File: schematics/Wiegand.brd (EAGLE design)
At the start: 79 x 51.9 mm, 88 parts, among them J1 AVR_SPI_PRG_6PTH, U1 MOC3063, U2 MOC3063, U3 V_REG_LDOSMD, U4 ATMEGA168, U5 MOC3063, U6 MOC3063, U7 MOC3063, U8 MOC3063, Y1 16Mhz

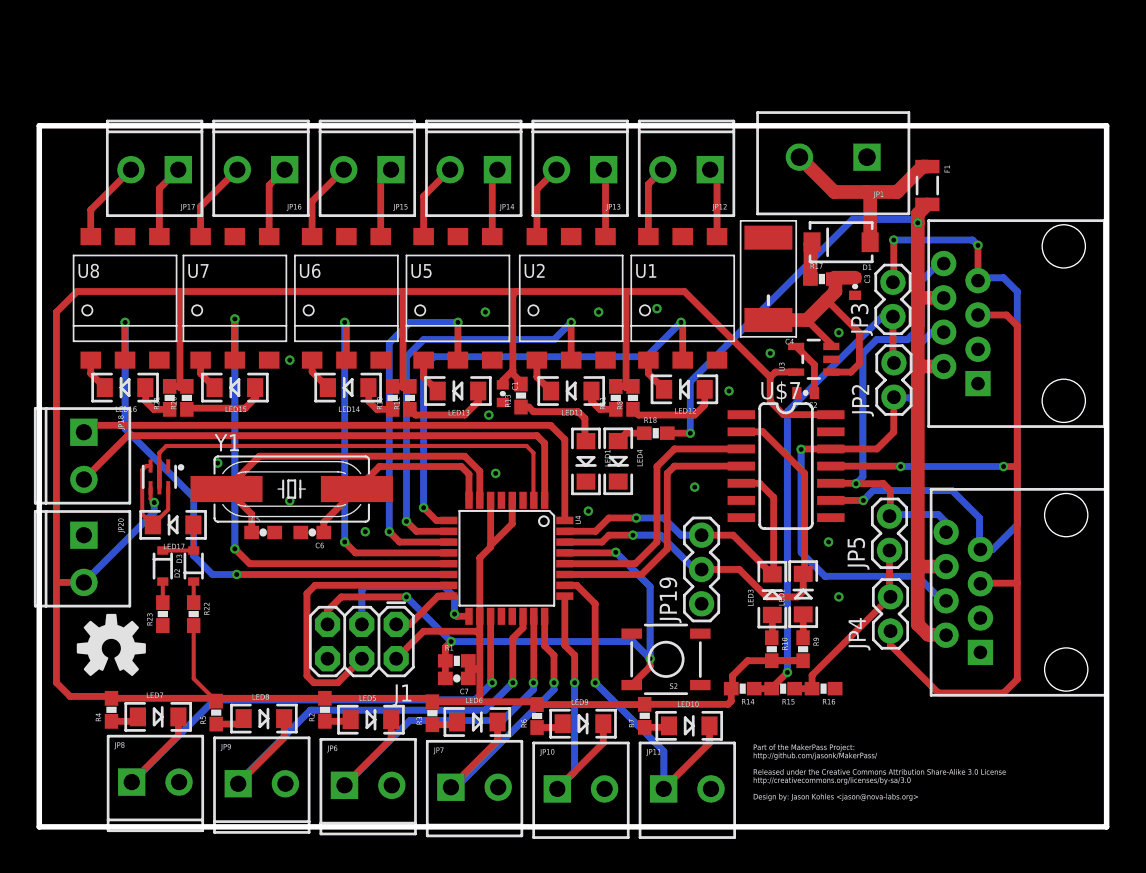
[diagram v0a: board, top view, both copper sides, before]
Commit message: updated schematics and added bom
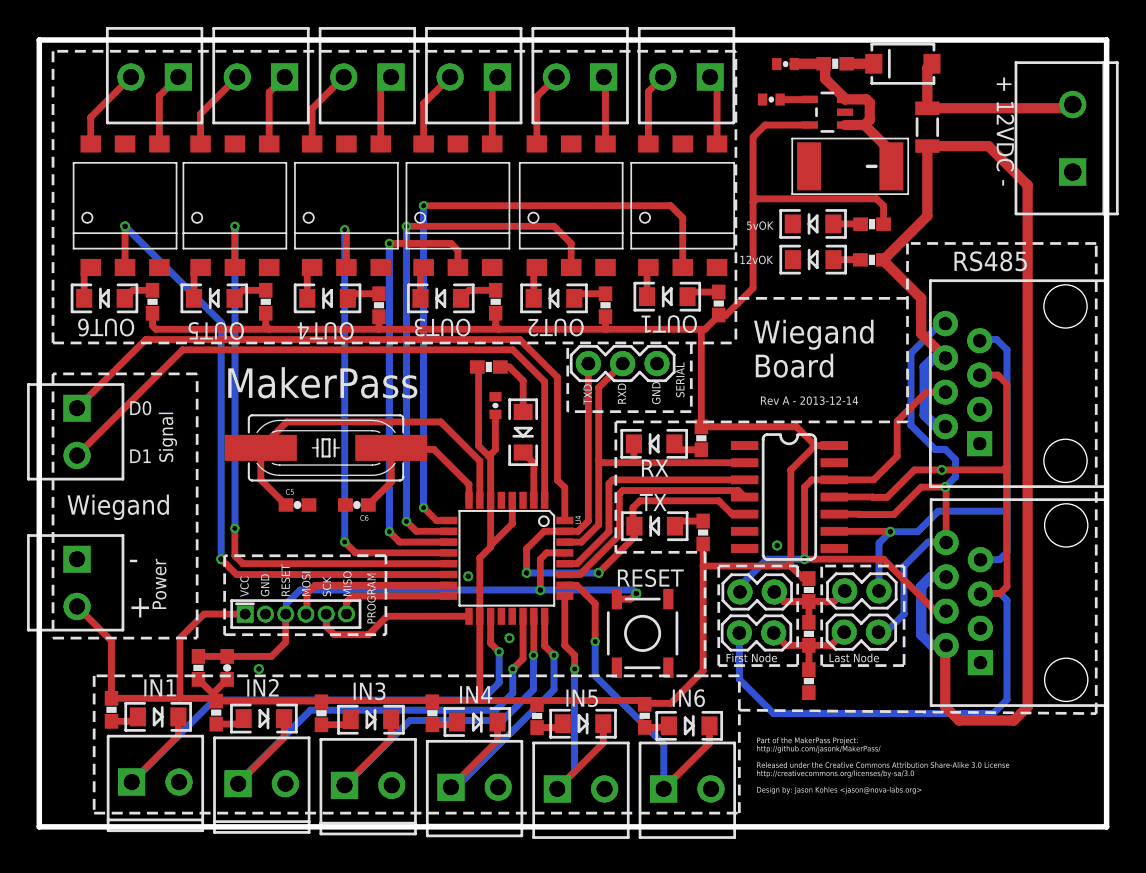
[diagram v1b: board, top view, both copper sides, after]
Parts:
- removed D2, D3: (no value), SparkFun-DiscreteSemi:SOD-323
- removed J1: AVR_SPI_PRG_6PTH, SparkFun:2X3
- removed LOGO1: OSHW-LOGOM, SparkFun-Aesthetics:OSHW-LOGO-M
- removed R23: 460, SparkFun:0603-RES
- JP18: value OUTPUT4 -> Wiegand-Signal
- JP20: value OUTPUT4 -> Wiegand-Power
- JP6, LED5: value INPUT1 -> INPUT3
- JP7, LED6: value INPUT2 -> INPUT4
- JP8, LED7: value INPUT3 -> INPUT1
- JP9, LED8: value INPUT4 -> INPUT2
- LED17: value STATUS LED (bicolor) -> STATUS
- R10, R9: value 220 -> 440
- R11, R12, R19, R2, R20, R21, R22, R3, R4, R5, R6, R7, R8: value 460 -> 440
- U$3: value BC847PN -> AVR_MINI_PROGSMD; device SparkFun-DiscreteSemi:SOT363 -> SparkFun-Connectors:AVR_MINI_PROG
- U3: value V_REG_LDOSMD -> MIC5219 5V; device SparkFun:SOT23-5 -> SparkFun-PowerIC:SOT23-5
- moved R13 28.9 mm to (61.6, 44.6), turned to 0 degrees
- moved R22 28.5 mm to (33.3, 34.0), turned to 180 degrees
- moved LED17 26.8 mm to (35.8, 29.2), turned to 270 degrees
- moved LED1 24.3 mm to (57.3, 44.6), turned to 180 degrees
- moved C2 21.9 mm to (54.2, 53.8)
- moved U$4 21.8 mm to (63.8, 21.1)
- moved LED4 20.8 mm to (57.3, 42.0), turned to 180 degrees
- moved JP3 20.6 mm to (59.6, 17.5), turned to 0 degrees
- moved R18 20.5 mm to (61.6, 42.0)
- moved R1 19.1 mm to (11.8, 11.8), turned to 270 degrees
- moved JP2 18.4 mm to (51.9, 17.4), turned to 0 degrees
- moved U3 18.3 mm to (58.3, 52.9)
- moved JP19 18.1 mm to (45.7, 34.3), turned to 180 degrees
- moved R9 17.3 mm to (49.0, 28.8), turned to 90 degrees
- moved C3 17.2 mm to (55.2, 56.5), turned to 180 degrees
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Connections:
- removed net N$42: D2.2, D3.1, LED17.A
- removed net N$43: D3.2, R23.2
- removed net N$44: LED17.C, U$3.3, U$3.6
- net GND: now also U$3.2; no longer J1.6, R23.1, U$3.1
- net INPUT1: now also JP8.1, LED7.C, U4.19; no longer JP6.1, LED5.C, U4.23
- net INPUT2: now also JP9.1, LED8.C, U4.22; no longer JP7.1, LED6.C, U4.24
- net INPUT3: now also JP6.1, LED5.C, U4.23; no longer JP8.1, LED7.C, U4.19
- net INPUT4: now also JP7.1, LED6.C, U4.24; no longer JP9.1, LED8.C, U4.22
- net MISO: now also U$3.6; no longer J1.1
- net MOSI: now also U$3.4; no longer J1.4
- net N$41: now also LED17.A; no longer D2.1
- net RESET: now also U$3.3; no longer J1.5
- net SCK: now also U$3.5; no longer J1.3
- net STATUS: now also LED17.C; no longer U$3.2, U$3.5
- net VCC: now also U$3.1; no longer J1.2, U$3.4
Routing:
- net STATUS: track 35.8 -> 3.87 mm
- net N$7: track 36.5 -> 7.37 mm, vias 1 -> 0
- net +12V: track 67.4 -> 92.8 mm, vias 2 -> 0
- net RS485-Y: track 50.8 -> 37.7 mm, vias 3 -> 1
- net INPUT1: track 28.6 -> 41.7 mm
- net TXD: track 26.1 -> 39.0 mm, vias 1 -> 2
- net INPUT2: track 22.6 -> 35.4 mm
- net INPUT4: track 35.0 -> 22.6 mm
- net INPUT3: track 41.0 -> 28.6 mm
- net OUTPUT1: track 35.9 -> 47.8 mm
- net VCC: track 234.6 -> 223.0 mm, vias 1 -> 0
- net MOSI: track 21.9 -> 12.3 mm
- net RS485-B: track 58.3 -> 67.5 mm, vias 2 -> 1
- net N$44: track 8.35 -> 0.00 mm
- net OUTPUT2: track 31.7 -> 39.8 mm
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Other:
- board size 79 x 51.9 mm -> 79 x 58.2 mm
- board text added: "+"
- board text added: "+ 12VDC -"
- board text added: "-"
- board text added: "12vOK"
- board text added: "5vOK"
- board text added: "D0"
- board text added: "D1"
- board text added: "First Node"
- board text added: "GND"
- board text added: "IN1"
- board text added: "IN2"
- board text added: "IN3"
- board text added: "IN4"
- board text added: "IN5"
- board text added: "IN6"
- board text added: "Last Node"
- board text added: "MISO"
- board text added: "MOSI"
- board text added: "MakerPass"
- board text added: "OUT1"
- board text added: "OUT2"
- board text added: "OUT3"
- board text added: "OUT4"
- board text added: "OUT5"
- board text added: "OUT6"
- board text added: "PROGRAM"
- board text added: "Power"
- board text added: "RESET"
- board text added: "RS485"
- board text added: "RX"
- board text added: "RXD"
- board text added: "Rev A - 2013-12-14"
- board text added: "SCK"
- board text added: "SERIAL"
- board text added: "Signal"
- board text added: "TX"
- board text added: "TXD"
- board text added: "VCC"
- board text added: "Wiegand"
- board text added: "Wiegand Board"

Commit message: update
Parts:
- removed JP20: Wiegand-Power, SparkFun:SCREWTERMINAL-3.5MM-2
- removed U$3: AVR_MINI_PROGSMD, SparkFun-Connectors:AVR_MINI_PROG
- removed U$7: RS485_SP491, SparkFun:SOIC-14
- added J1: AVR_SPI_PRG_6NS, SparkFun-Connectors:2X3-NS
- added JP21: SERIAL, SparkFun-Connectors:1X03
- added U9: MOC3063, SparkFun-DiscreteSemi:DIP8SMD
- C1, C2, C3: device SparkFun:0402-CAP -> SparkFun-Capacitors:0603-CAP
- C4: device SparkFun:VISHAY_C -> SparkFun-Capacitors:PANASONIC_D
- JP19: value SERIAL -> Wiegand-Power; device SparkFun-Connectors:1X03 -> SparkFun:SCREWTERMINAL-3.5MM-2
- LED1, LED10, LED11, LED12, LED13, LED14, LED15, LED16, LED17, LED2, LED3, LED4, LED5, LED6, LED7, LED8, LED9: device SparkFun:LED-1206 -> dp_devices:LED-805
- U1: value MOC3063 -> ATMEGA168; device SparkFun-DiscreteSemi:DIP8SMD -> SparkFun-DigitalIC:TQFP32-08
- U2: value MOC3063 -> RS485_SP491; device SparkFun-DiscreteSemi:DIP8SMD -> SparkFun:SOIC-14
- U4: value ATMEGA168 -> MOC3063; device SparkFun:TQFP32-08 -> SparkFun-DiscreteSemi:DIP8SMD
- moved JP19 45.3 mm to (2.79, 19.8), turned to 270 degrees
- moved R1 35.0 mm to (46.1, 18.4), turned to 0 degrees
- moved C7 33.4 mm to (46.1, 20.5), turned to 180 degrees
- moved U2 29.9 mm to (59.3, 23.8), turned to 270 degrees
- moved U1 29.2 mm to (34.6, 19.9), turned to 270 degrees
- moved U4 29.2 mm to (47.6, 46.0), turned to 0 degrees
- moved U5 8.38 mm to (39.4, 46.0)
- moved U7 8.26 mm to (22.7, 46.0)
- moved U6 8.25 mm to (31.0, 46.0)
- moved U8 8.13 mm to (14.5, 46.0)
- moved LED2 6.97 mm to (52.5, 28.1), turned to 90 degrees
- moved LED3 6.95 mm to (52.5, 21.8), turned to 90 degrees
- moved F1 5.72 mm to (67.3, 46.3), turned to 180 degrees
- moved C4 5.29 mm to (64.6, 51.5), turned to 180 degrees
- moved R10 3.85 mm to (52.5, 20.0), turned to 180 degrees
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- renumbered U$1 to X1, U$2 to X2
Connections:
- net D0: now also U1.32; no longer U4.32
- net D1: now also U1.1; no longer U4.1
- net DE: now also U1.27, U2.4; no longer U$7.4, U4.27
- net GND: now also J1.6, JP21.1, U1.21, U1.3, U1.5, U2.6, U2.7; no longer JP20.1, U$3.2, U$7.6, U$7.7, U4.21, U4.3, U4.5
- net INPUT1: now also U1.19; no longer U4.19
- net INPUT2: now also U1.22; no longer U4.22
- net INPUT3: now also U1.23; no longer U4.23
- net INPUT4: now also U1.24; no longer U4.24
- net INPUT5: now also U1.25; no longer U4.25
- net INPUT6: now also U1.26; no longer U4.26
- net MISO: now also J1.1, U1.16; no longer U$3.6, U4.16
- net MOSI: now also J1.4, U1.15; no longer U$3.4, U4.15
- net N$100: now also U1.7; no longer U4.7
- net N$101: now also U1.8; no longer U4.8
- net N$15: now also U4.1; no longer U1.1
- net N$17: now also U4.4; no longer U1.4
- net N$18: now also U4.6; no longer U1.6
- net N$19: now also U5.4; no longer U2.4
- net N$20: now also U5.6; no longer U2.6
- net N$22: now also U5.1; no longer U2.1
- net N$23: now also U6.4; no longer U5.4
- net N$24: now also U6.6; no longer U5.6
- net N$28: now also U6.1; no longer U5.1
- net N$29: now also U7.4; no longer U6.4
- net N$30: now also U7.6; no longer U6.6
- net N$32: now also U7.1; no longer U6.1
- net N$33: now also U8.4; no longer U7.4
- net N$34: now also U8.6; no longer U7.6
- net N$36: now also U8.1; no longer U7.1
- net N$37: now also U9.4; no longer U8.4
- net N$38: now also U9.6; no longer U8.6
- net N$40: now also U9.1; no longer U8.1
- net OUTPUT1: now also U1.9, U4.2; no longer U1.2, U4.9
- net OUTPUT2: now also U1.10, U5.2; no longer U2.2, U4.10
- net OUTPUT3: now also U1.11, U6.2; no longer U4.11, U5.2
- net OUTPUT4: now also U1.12, U7.2; no longer U4.12, U6.2
- net OUTPUT5: now also U1.13, U8.2; no longer U4.13, U7.2
- net OUTPUT6: now also U1.14, U9.2; no longer U4.14, U8.2
- net RE: now also U1.28, U2.3; no longer U$7.3, U4.28
- net RESET: now also J1.5, U1.29; no longer U$3.3, U4.29
- net RS485-A: now also U2.12; no longer U$7.12
- net RS485-B: now also U2.11; no longer U$7.11
- net RS485-Y: now also U2.9; no longer U$7.9
- net RS485-Z: now also U2.10; no longer U$7.10
- net RXD: now also JP21.2, U1.30, U2.2; no longer JP19.2, U$7.2, U4.30
- net SCK: now also J1.3, U1.17; no longer U$3.5, U4.17
- net STATUS: now also U1.2; no longer U4.2
- net TXD: now also JP21.3, U1.31, U2.5; no longer JP19.3, U$7.5, U4.31
- net VCC: now also J1.2, JP19.2, U1.18, U1.4, U1.6, U2.14; no longer JP20.2, U$3.1, U$7.14, U4.18, U4.4, U4.6
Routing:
- net VCC: track 223.0 -> 243.1 mm, vias 0 -> 2
- net MISO: track 8.64 -> 20.4 mm, vias 0 -> 1
- net +12V: track 92.8 -> 81.1 mm
- net RESET: track 42.1 -> 31.4 mm
- net 12V_IN: track 14.3 -> 22.5 mm
- net INPUT5: track 21.3 -> 29.4 mm
- net TXD: track 39.0 -> 43.8 mm
- net RS485-B: track 67.5 -> 62.9 mm
- net INPUT4: track 22.6 -> 27.0 mm
- net RE: track 18.0 -> 22.4 mm
- net INPUT3: track 28.6 -> 33.0 mm
- net DE: track 17.9 -> 21.9 mm
- net INPUT2: track 35.4 -> 39.3 mm
- net N$4: track 14.5 -> 10.8 mm
- net RXD: track 28.0 -> 31.6 mm
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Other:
- board text added: "Rev A - 2013-12-17"
- board text removed: "MISO"
- board text removed: "MOSI"
- board text removed: "PROGRAM"
- board text removed: "Rev A - 2013-12-14"
- board text removed: "SCK"
- board text removed: "VCC"

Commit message: Board Rev B
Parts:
- removed C1: 2.2uF Tantalum, SparkFun-Capacitors:0603-CAP
- removed C3: 0.1uF 50V, SparkFun-Capacitors:0603-CAP
- removed D1: (no value), SparkFun:SMA-DIODE
- removed F1: PTCSMD, SparkFun:PTC-1206
- removed JP1: 12VDC, SparkFun:SCREWTERMINAL-5MM-2
- removed JP10: INPUT5, SparkFun:SCREWTERMINAL-3.5MM-2
- removed JP11: INPUT6, SparkFun:SCREWTERMINAL-3.5MM-2
- removed JP12: OUTPUT1, SparkFun:SCREWTERMINAL-3.5MM-2
- removed JP13: OUTPUT2, SparkFun:SCREWTERMINAL-3.5MM-2
- removed JP14: OUTPUT3, SparkFun:SCREWTERMINAL-3.5MM-2
- removed JP15: OUTPUT4, SparkFun:SCREWTERMINAL-3.5MM-2
- removed JP16: OUTPUT5, SparkFun:SCREWTERMINAL-3.5MM-2
- removed JP17: OUTPUT6, SparkFun:SCREWTERMINAL-3.5MM-2
- removed JP18: Wiegand-Signal, SparkFun:SCREWTERMINAL-3.5MM-2
- removed JP19: Wiegand-Power, SparkFun:SCREWTERMINAL-3.5MM-2
- removed JP21: SERIAL, SparkFun-Connectors:1X03
- removed JP6: INPUT3, SparkFun:SCREWTERMINAL-3.5MM-2
- removed JP7: INPUT4, SparkFun:SCREWTERMINAL-3.5MM-2
- removed JP8: INPUT1, SparkFun:SCREWTERMINAL-3.5MM-2
- removed JP9: INPUT2, SparkFun:SCREWTERMINAL-3.5MM-2
- removed U3: MIC5219 5V, SparkFun-PowerIC:SOT23-5
- added IC1: (no value), linear:SOT223
- added Q1, Q2: NTR1P02T1G, SparkFun:SOT23-3
- added R23: 10K, SparkFun:0603-RES
- added X3: (no value), LumisenseV6:CON-1X12-TERMBLOCK-3.5MM
- C2: value 470pF -> 100nF; device SparkFun-Capacitors:0603-CAP -> SparkFun:0603-CAP
- C4: value 220uF 35V -> 47uF; device SparkFun-Capacitors:PANASONIC_D -> rcl:PANASONIC_D
- JP2: value First Node -> First Node A
- JP3: value Last Node -> Last Node Y
- JP4: value First Node -> First Node B
- JP5: value Last Node -> Last Node Z
- LED1: value 5V OK -> GRN
- LED10: value INPUT6 -> RED
- LED11: value OUTPUT2 -> RED
- LED12: value OUTPUT1 -> RED
- LED13: value OUTPUT3 -> RED
- LED14: value OUTPUT4 -> RED
- LED15: value OUTPUT5 -> RED
- LED16: value OUTPUT6 -> RED
- LED17: value STATUS -> YLW
- LED2: value RX -> RED
- LED3: value TX -> RED
- LED4: value 12V OK -> GRN
- LED5: value INPUT3 -> RED
- LED6: value INPUT4 -> RED
- LED7: value INPUT1 -> RED
- LED8: value INPUT2 -> RED
- LED9: value INPUT5 -> RED
- R17: value 12 ohm 5 watt -> 10K
- X1, X2: value RJ45-8PTH -> (none); device SparkFun:RJ45-8 -> LumisenseV6:CON-1X12-TERMBLOCK-3.5MM
- moved X2 71.6 mm to (9.00, 7.30), turned to 0 degrees
- moved C2 53.6 mm to (22.1, 12.7), turned to 180 degrees
- moved U$4 47.5 mm to (26.9, 51.1), turned to 270 degrees
- moved X1 46.3 mm to (46.5, 52.3), turned to 180 degrees
- moved R17 41.7 mm to (33.8, 22.4), turned to 90 degrees
- moved C6 19.9 mm to (5.08, 31.2), turned to 90 degrees
- moved J1 16.0 mm to (6.35, 14.7)
- moved LED2 12.6 mm to (39.9, 28.7)
- moved JP4 12.5 mm to (63.8, 12.4), turned to 180 degrees
- moved LED3 12.3 mm to (40.1, 21.6)
- moved R1 12.2 mm to (34.0, 16.8), turned to 270 degrees
- moved C7 11.0 mm to (35.8, 16.8), turned to 90 degrees
- moved R4 10.8 mm to (12.5, 2.63), turned to 0 degrees
- moved R10 10.2 mm to (42.7, 22.6), turned to 90 degrees
- moved LED1 10.1 mm to (65.5, 40.4), turned to 270 degrees
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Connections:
- removed net 12V_IN: D1.A, F1.1, JP1.2
- new net N$42: Q2.1, R23.1
- net +12V: now also C4.+, IC1.3, X3.10; no longer F1.2, X1.2, X1.6, X2.2, X2.6
- net D0: now also X3.7; no longer JP18.1
- net D1: now also X3.8; no longer JP18.2
- net GND: now also IC1.1, Q1.3, Q2.3, X2.10, X2.12, X2.2, X2.4, X2.6, X2.8, X3.11, X3.12; no longer C1.2, C3.2, JP1.1, JP10.2, JP11.2, JP19.1, JP21.1, JP6.2, JP7.2, JP8.2, JP9.2, U3.2, X1.1, X1.3, X2.1, X2.3
- net INPUT1: now also X2.1; no longer JP8.1
- net INPUT2: now also X2.3; no longer JP9.1
- net INPUT3: now also X2.5; no longer JP6.1
- net INPUT4: now also X2.7; no longer JP7.1
- net INPUT5: now also X2.9; no longer JP10.1
- net INPUT6: now also X2.11; no longer JP11.1
- net N$17: now also X1.1; no longer JP12.1
- net N$18: now also X1.2; no longer JP12.2
- net N$19: now also X1.3; no longer JP13.1
- net N$20: now also X1.4; no longer JP13.2
- net N$23: now also X1.5; no longer JP14.1
- net N$24: now also X1.6; no longer JP14.2
- net N$29: now also X1.7; no longer JP15.1
- net N$3: now also U8.4, X1.9; no longer C2.1, U3.4
- net N$30: now also X1.8; no longer JP15.2
- net N$33: now also LED2.C, Q2.2; no longer JP16.1, U8.4
- net N$34: now also Q1.1, R17.1; no longer JP16.2, U8.6
- net N$37: now also X1.11; no longer JP17.1
- net N$38: now also X1.12; no longer JP17.2
- net N$4: now also U8.6, X1.10; no longer C3.1, C4.+, R17.2, U3.1, U3.3
- net N$9: now also LED3.C, Q1.2; no longer D1.C, R17.1
- net RS485-A: now also X3.4; no longer X1.4, X2.4
- net RS485-B: now also X3.3; no longer X1.5, X2.5
- net RS485-Y: now also X3.1; no longer X1.7, X2.7
- net RS485-Z: now also X3.2; no longer X1.8, X2.8
- net RXD: now also R17.2, X3.5; no longer JP21.2, LED2.C
- net TXD: now also R23.2, X3.6; no longer JP21.3, LED3.C
- net VCC: now also C2.1, IC1.2, IC1.4, X3.9; no longer C1.1, JP19.2, U3.5
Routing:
- net VCC: track 243.1 -> 342.5 mm
- net +12V: track 81.1 -> 23.4 mm
- net RXD: track 31.6 -> 79.5 mm, vias 0 -> 1
- net RS485-B: track 62.9 -> 27.7 mm, vias 1 -> 0
- net TXD: track 43.8 -> 78.2 mm, vias 2 -> 1
- net OUTPUT3: track 32.6 -> 64.8 mm
- net OUTPUT2: track 39.8 -> 70.6 mm
- net OUTPUT1: track 47.8 -> 78.6 mm
- net OUTPUT4: track 34.0 -> 57.1 mm
- net 12V_IN: track 22.5 -> 0.00 mm
- net INPUT1: track 44.8 -> 27.2 mm, vias 1 -> 0
- net INPUT2: track 39.3 -> 22.1 mm, vias 1 -> 0
- net INPUT3: track 33.0 -> 16.0 mm, vias 1 -> 0
- net RESET: track 31.4 -> 45.9 mm
- net N$100: track 26.1 -> 12.5 mm
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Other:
- board size 79 x 58.2 mm -> 78.7 x 58.4 mm
- board text added: "12V"
- board text added: "5V"
- board text added: "A"
- board text added: "B"
- board text added: "Design by: Jason Kohles <jason@nova-labs.org> Ted Markson <ted@nova-labs.org>"
- board text added: "Part of the MakerPass Project: http://github.com/jasonk/MakerPass/ Released under the Creative Commons Attribution Share-Alike 3.0 License http://creativecommons.org/licenses/by-sa/3.0"
- board text added: "Rev B - 2014-01-01"
- board text added: "Status"
- board text added: "Y"
- board text added: "Z"
- board text removed: "+"
- board text removed: "+ 12VDC -"
- board text removed: "-"
- board text removed: "Part of the MakerPass Project: http://github.com/jasonk/MakerPass/ Released under the Creative Commons Attribution Share-Alike 3.0 License http://creativecommons.org/licenses/by-sa/3.0 Design by: Jason Kohles <jason@nova-labs.org>"
- board text removed: "Power"
- board text removed: "RS485"
- board text removed: "Rev A - 2013-12-17"
- board text removed: "SERIAL"
- board text removed: "Signal"
- board text removed: "Wiegand"
